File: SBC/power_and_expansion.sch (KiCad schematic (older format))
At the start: 19 parts, among them J1 VCC1, J10 GND3, J11 Expansion Bus, J2 GND1, J3 VCC2, J4 POWER, J5 GND2, J8 JTAG, J9 VCC3

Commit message: Preparation for Pluto v3.0
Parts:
- removed J8: JTAG, Connectors_IDC:IDC-Header_2x05_Pitch2.54mm_Straight, symbol conn:CONN_02X05
- removed MK2, MK5: Mounting_Hole, Mounting_Holes:MountingHole_3.2mm_M3_Pad, symbol mechanical:Mounting_Hole
- F1: footprint Fuse_Holders_and_Fuses:Fuseholder5x20_horiz_open_Schurter_0031_8201 -> Fuse:Fuseholder_Cylinder-5x20mm_Schurter_0031_8201_Horizontal_Open; symbol device:Fuse_Small -> pluto-rescue:Fuse_Small-device
- J1, J10, J2, J3, J5, J9: footprint Pin_Headers:Pin_Header_Straight_1x01_Pitch2.54mm -> Connector_PinHeader_2.54mm:PinHeader_1x01_P2.54mm_Vertical; symbol conn:TEST_1P -> pluto-rescue:TEST_1P-conn
- J11: footprint Connectors_IDC:IDC-Header_2x20_Pitch2.54mm_Straight -> Connector_IDC:IDC-Header_2x20_P2.54mm_Vertical
- J4: footprint Connectors_Molex:Molex_NanoFit_1x04x2.50mm_Angled -> Connector_Molex:Molex_Nano-Fit_105313-xx04_1x04_P2.50mm_Horizontal; symbol conn:CONN_01X04 -> pluto-rescue:CONN_01X04-conn
- MK1, MK3, MK4, MK6: footprint Mounting_Holes:MountingHole_3.2mm_M3_Pad -> MountingHole:MountingHole_3.2mm_M3_Pad; symbol mechanical:Mounting_Hole -> pluto-rescue:Mounting_Hole-mechanical
- R1: footprint Resistors_ThroughHole:R_Axial_DIN0411_L9.9mm_D3.6mm_P12.70mm_Horizontal -> Resistor_THT:R_Axial_DIN0411_L9.9mm_D3.6mm_P7.62mm_Vertical; symbol device:R_Small -> pluto-rescue:R_Small-device
- S1: symbol standard:SPDT -> pluto-rescue:SPDT-standard
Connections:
- net labels added: ~IO
- net labels removed: TCK, TDI, TDO, TMS, ~7FAX, ~7FCX
- wire segments 67 -> 56
- no-connect marks 6 -> 5
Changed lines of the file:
@@
 EESchema Schematic File Version 4
 LIBS:pluto-cache
-EELAYER 29 0
+EELAYER 30 0
 EELAYER END
 $Descr A4 11693 8268
@@
 $EndDescr
 $Comp
-L mechanical:Mounting_Hole MK2
-U 1 1 59149E60
-P 1825 3025
-F 0 "MK2" H 1825 3225 50  0000 C CNN
-F 1 "Mounting_Hole" H 1825 3150 50  0000 C CNN
-F 2 "Mounting_Holes:MountingHole_3.2mm_M3_Pad" H 1825 3025 50  0001 C CNN
-F 3 "" H 1825 3025 50  0001 C CNN
-	1    1825 3025
-	1    0    0    -1
-$EndComp
-$Comp
-L mechanical:Mounting_Hole MK3
+L pluto-rescue:Mounting_Hole-mechanical MK3
 U 1 1 59149E83
 P 1825 3450
 F 0 "MK3" H 1825 3650 50  0000 C CNN
 F 1 "Mounting_Hole" H 1825 3575 50  0000 C CNN
-F 2 "Mounting_Holes:MountingHole_3.2mm_M3_Pad" H 1825 3450 50  0001 C CNN
+F 2 "MountingHole:MountingHole_3.2mm_M3_Pad" H 1825 3450 50  0001 C CNN
 F 3 "" H 1825 3450 50  0001 C CNN
 	1    1825 3450
@@
 $EndComp
 $Comp
-L mechanical:Mounting_Hole MK1
+L pluto-rescue:Mounting_Hole-mechanical MK1
 U 1 1 5932DD04
-P 1125 3950
-F 0 "MK1" H 1125 4150 50  0000 C CNN
-F 1 "Mounting_Hole" H 1125 4075 50  0000 C CNN
-F 2 "Mounting_Holes:MountingHole_3.2mm_M3_Pad" H 1125 3950 50  0001 C CNN
-F 3 "" H 1125 3950 50  0001 C CNN
-	1    1125 3950
-	1    0    0    -1
-$EndComp
-$Comp
-L mechanical:Mounting_Hole MK4
+P 2625 3925
+F 0 "MK1" H 2625 4125 50  0000 C CNN
+F 1 "Mounting_Hole" H 2625 4050 50  0000 C CNN
+F 2 "MountingHole:MountingHole_3.2mm_M3_Pad" H 2625 3925 50  0001 C CNN
+F 3 "" H 2625 3925 50  0001 C CNN
+	1    2625 3925
+	1    0    0    -1
+$EndComp
+$Comp
+L pluto-rescue:Mounting_Hole-mechanical MK4
 U 1 1 5932DD62
 P 1825 3950
 F 0 "MK4" H 1825 4150 50  0000 C CNN
 F 1 "Mounting_Hole" H 1825 4075 50  0000 C CNN
-F 2 "Mounting_Holes:MountingHole_3.2mm_M3_Pad" H 1825 3950 50  0001 C CNN
+F 2 "MountingHole:MountingHole_3.2mm_M3_Pad" H 1825 3950 50  0001 C CNN
 F 3 "" H 1825 3950 50  0001 C CNN
 	1    1825 3950
@@
 $EndComp
 $Comp
-L conn:CONN_02X05 J8
-U 1 1 59F22BEE
-P 4275 3000
-F 0 "J8" H 4275 3300 50  0000 C CNN
-F 1 "JTAG" H 4275 2700 50  0000 C CNN
-F 2 "Connectors_IDC:IDC-Header_2x05_Pitch2.54mm_Straight" H 4275 1800 50  0001 C CNN
-F 3 "" H 4275 1800 50  0001 C CNN
-	1    4275 3000
-	1    0    0    -1
-$EndComp
-Text HLabel 3775 3000 0    60   Output ~ 0
-TDI
-Text HLabel 3775 3100 0    60   Input ~ 0
-TDO
-Text HLabel 3775 2800 0    60   Output ~ 0
-TCK
-Text HLabel 3775 2900 0    60   Output ~ 0
-TMS
-Wire Wire Line
-	3775 2800 4025 2800
-Wire Wire Line
-	3775 2900 4025 2900
-Wire Wire Line
-	3775 3000 4025 3000
-Wire Wire Line
-	3775 3100 4025 3100
-Wire Wire Line
-	4525 2800 4775 2800
-Wire Wire Line
-	4775 2900 4525 2900
-Wire Wire Line
-	4525 3000 4900 3000
-Wire Wire Line
-	4775 3100 4525 3100
-Wire Wire Line
-	4775 2675 4775 2800
-Connection ~ 4775 2800
-$Comp
-L power:GND #PWR024
-U 1 1 59F407A0
-P 4775 2675
-F 0 "#PWR024" H 4775 2425 50  0001 C CNN
-F 1 "GND" H 4775 2525 50  0000 C CNN
-F 2 "" H 4775 2675 50  0001 C CNN
-F 3 "" H 4775 2675 50  0001 C CNN
-	1    4775 2675
-	-1   0    0    1
-$EndComp
-$Comp
-L power:VCC #PWR025
-U 1 1 59F407C6
-P 4900 3000
-F 0 "#PWR025" H 4900 2850 50  0001 C CNN
-F 1 "VCC" V 4900 3175 50  0000 C CNN
-F 2 "" H 4900 3000 50  0001 C CNN
-F 3 "" H 4900 3000 50  0001 C CNN
-	1    4900 3000
-	0    1    1    0
-$EndComp
-Connection ~ 4775 2900
-NoConn ~ 4525 3200
-NoConn ~ 4025 3200
-$Comp
-L mechanical:Mounting_Hole MK5
-U 1 1 59F424EE
-P 2600 3000
-F 0 "MK5" H 2600 3200 50  0000 C CNN
-F 1 "Mounting_Hole" H 2600 3125 50  0000 C CNN
-F 2 "Mounting_Holes:MountingHole_3.2mm_M3_Pad" H 2600 3000 50  0001 C CNN
-F 3 "" H 2600 3000 50  0001 C CNN
-	1    2600 3000
-	1    0    0    -1
-$EndComp
-$Comp
-L mechanical:Mounting_Hole MK6
+L pluto-rescue:Mounting_Hole-mechanical MK6
 U 1 1 59F42548
 P 2600 3350
 F 0 "MK6" H 2600 3550 50  0000 C CNN
 F 1 "Mounting_Hole" H 2600 3475 50  0000 C CNN
-F 2 "Mounting_Holes:MountingHole_3.2mm_M3_Pad" H 2600 3350 50  0001 C CNN
+F 2 "MountingHole:MountingHole_3.2mm_M3_Pad" H 2600 3350 50  0001 C CNN
 F 3 "" H 2600 3350 50  0001 C CNN
 	1    2600 3350
@@
 $EndComp
 $Comp
-L conn:CONN_01X04 J4
+L pluto-rescue:CONN_01X04-conn J4
 U 1 1 5A1609CD
 P 7650 1725
 F 0 "J4" H 7650 1975 50  0000 C CNN
 F 1 "POWER" V 7750 1725 50  0000 C CNN
-F 2 "Connectors_Molex:Molex_NanoFit_1x04x2.50mm_Angled" H 7650 1725 50  0001 C CNN
+F 2 "Connector_Molex:Molex_Nano-Fit_105313-xx04_1x04_P2.50mm_Horizontal" H 7650 1725 50  0001 C CNN
 F 3 "" H 7650 1725 50  0001 C CNN
 	1    7650 1725
@@
 Connection ~ 7375 1675
 $Comp
-L device:Fuse_Small F1
+L pluto-rescue:Fuse_Small-device F1
 U 1 1 5A30BB96
 P 6800 1575
 F 0 "F1" H 6800 1515 50  0000 C CNN
 F 1 "1Amp" H 6800 1635 50  0000 C CNN
-F 2 "Fuse_Holders_and_Fuses:Fuseholder5x20_horiz_open_Schurter_0031_8201" H 6800 1575 50  0001 C CNN
+F 2 "Fuse:Fuseholder_Cylinder-5x20mm_Schurter_0031_8201_Horizontal_Open" H 6800 1575 50  0001 C CNN
 F 3 "" H 6800 1575 50  0001 C CNN
 	1    6800 1575
@@
 $EndComp
 $Comp
-L standard:SPDT S1
+L pluto-rescue:SPDT-standard S1
 U 1 1 5A30BD5A
 P 6425 1625
@@
 $EndComp
 $Comp
-L device:R_Small R1
+L pluto-rescue:R_Small-device R1
 U 1 1 5A30C649
 P 5625 1625
 F 0 "R1" V 5700 1575 50  0000 L CNN
 F 1 "1kOhm" V 5525 1525 50  0000 L CNN
-F 2 "Resistors_ThroughHole:R_Axial_DIN0411_L9.9mm_D3.6mm_P12.70mm_Horizontal" H 5625 1625 50  0001 C CNN
+F 2 "Resistor_THT:R_Axial_DIN0411_L9.9mm_D3.6mm_P7.62mm_Vertical" H 5625 1625 50  0001 C CNN
 F 3 "" H 5625 1625 50  0001 C CNN
 	1    5625 1625
@@
 	5425 1625 5525 1625
 $Comp
-L conn:TEST_1P J1
+L pluto-rescue:TEST_1P-conn J1
 U 1 1 5A30C731
 P 1450 5025
 F 0 "J1" H 1450 5295 50  0000 C CNN
 F 1 "VCC1" H 1450 5225 50  0000 C CNN
-F 2 "Pin_Headers:Pin_Header_Straight_1x01_Pitch2.54mm" H 1650 5025 50  0001 C CNN
+F 2 "Connector_PinHeader_2.54mm:PinHeader_1x01_P2.54mm_Vertical" H 1650 5025 50  0001 C CNN
 F 3 "" H 1650 5025 50  0001 C CNN
 	1    1450 5025
@@
 $EndComp
 $Comp
-L conn:TEST_1P J3
+L pluto-rescue:TEST_1P-conn J3
 U 1 1 5A30C776
 P 1775 5025
 F 0 "J3" H 1775 5295 50  0000 C CNN
 F 1 "VCC2" H 1775 5225 50  0000 C CNN
-F 2 "Pin_Headers:Pin_Header_Straight_1x01_Pitch2.54mm" H 1975 5025 50  0001 C CNN
+F 2 "Connector_PinHeader_2.54mm:PinHeader_1x01_P2.54mm_Vertical" H 1975 5025 50  0001 C CNN
 F 3 "" H 1975 5025 50  0001 C CNN
 	1    1775 5025
@@
 $EndComp
 $Comp
-L conn:TEST_1P J9
+L pluto-rescue:TEST_1P-conn J9
 U 1 1 5A30C7BB
 P 2125 5025
 F 0 "J9" H 2125 5295 50  0000 C CNN
 F 1 "VCC3" H 2125 5225 50  0000 C CNN
-F 2 "Pin_Headers:Pin_Header_Straight_1x01_Pitch2.54mm" H 2325 5025 50  0001 C CNN
+F 2 "Connector_PinHeader_2.54mm:PinHeader_1x01_P2.54mm_Vertical" H 2325 5025 50  0001 C CNN
 F 3 "" H 2325 5025 50  0001 C CNN
 	1    2125 5025
@@
 $EndComp
 $Comp
-L conn:TEST_1P J2
+L pluto-rescue:TEST_1P-conn J2
 U 1 1 5A30C814
 P 1450 5625
 F 0 "J2" H 1450 5895 50  0000 C CNN
 F 1 "GND1" H 1450 5825 50  0000 C CNN
-F 2 "Pin_Headers:Pin_Header_Straight_1x01_Pitch2.54mm" H 1650 5625 50  0001 C CNN
+F 2 "Connector_PinHeader_2.54mm:PinHeader_1x01_P2.54mm_Vertical" H 1650 5625 50  0001 C CNN
 F 3 "" H 1650 5625 50  0001 C CNN
 	1    1450 5625
@@
 $EndComp
 $Comp
-L conn:TEST_1P J5
+L pluto-rescue:TEST_1P-conn J5
 U 1 1 5A30C853
 P 1775 5625
 F 0 "J5" H 1775 5895 50  0000 C CNN
 F 1 "GND2" H 1775 5825 50  0000 C CNN
-F 2 "Pin_Headers:Pin_Header_Straight_1x01_Pitch2.54mm" H 1975 5625 50  0001 C CNN
+F 2 "Connector_PinHeader_2.54mm:PinHeader_1x01_P2.54mm_Vertical" H 1975 5625 50  0001 C CNN
 F 3 "" H 1975 5625 50  0001 C CNN
 	1    1775 5625
@@
 $EndComp
 $Comp
-L conn:TEST_1P J10
+L pluto-rescue:TEST_1P-conn J10
 U 1 1 5A30C89C
 P 2125 5625
 F 0 "J10" H 2125 5895 50  0000 C CNN
 F 1 "GND3" H 2125 5825 50  0000 C CNN
-F 2 "Pin_Headers:Pin_Header_Straight_1x01_Pitch2.54mm" H 2325 5625 50  0001 C CNN
+F 2 "Connector_PinHeader_2.54mm:PinHeader_1x01_P2.54mm_Vertical" H 2325 5625 50  0001 C CNN
 F 3 "" H 2325 5625 50  0001 C CNN
 	1    2125 5625
@@
 Text Label 6950 1575 0    60   ~ 0
 PWR_IN
-Text HLabel 9400 4775 2    60   Output ~ 0
-~7FCX
-Text HLabel 9400 4875 2    60   Output ~ 0
-~7FAX
 Text HLabel 8100 4875 0    60   Input ~ 0
 ~IRQ
@@
 F 0 "J11" H 8750 5075 50  0000 C CNN
 F 1 "Expansion Bus" V 8750 3925 50  0000 C CNN
-F 2 "Connectors_IDC:IDC-Header_2x20_Pitch2.54mm_Straight" H 8700 4075 50  0001 C CNN
+F 2 "Connector_IDC:IDC-Header_2x20_P2.54mm_Vertical" H 8700 4075 50  0001 C CNN
 F 3 "" H 8700 4075 50  0001 C CNN
 	1    8700 4075
@@
 Wire Wire Line
 	9000 4775 9400 4775
-Wire Wire Line
-	9000 4875 9400 4875
 Wire Wire Line
 	9000 4975 9400 4975
@@
 D7
 Wire Wire Line
-	4775 2800 4775 2900
-Wire Wire Line
-	4775 2900 4775 3100
-Wire Wire Line
 	7275 1675 7375 1675
 Wire Wire Line
@@
 Wire Wire Line
 	8750 5475 9000 5475
+NoConn ~ 9000 4875
+Text HLabel 9400 4775 2    60   Output ~ 0
+~IO
+$Comp
+L power:PWR_FLAG #FLG0101
+U 1 1 5D7FB0B7
+P 6200 1800
+F 0 "#FLG0101" H 6200 1875 50  0001 C CNN
+F 1 "PWR_FLAG" H 6200 1973 50  0000 C CNN
+F 2 "" H 6200 1800 50  0001 C CNN
+F 3 "~" H 6200 1800 50  0001 C CNN
+	1    6200 1800
+	-1   0    0    1
+$EndComp
+Wire Wire Line
+	6200 1800 6200 1625
 Wire Bus Line
 	9500 3175 9500 3875

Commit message: A better layout of PCB.
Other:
- note added: "IO ($7F60)"
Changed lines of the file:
@@
 Wire Bus Line
 	8000 3175 8000 4675
+Text Notes 9625 4825 0    60   ~ 12
+IO ($7F60)
 $EndSCHEMATC

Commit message: Converting to SMD of almost all components.
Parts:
- R1: footprint Resistor_THT:R_Axial_DIN0411_L9.9mm_D3.6mm_P7.62mm_Vertical -> Resistor_SMD:R_1206_3216Metric_Pad1.42x1.75mm_HandSolder
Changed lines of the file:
@@
 F 0 "R1" V 5700 1575 50  0000 L CNN
 F 1 "1kOhm" V 5525 1525 50  0000 L CNN
-F 2 "Resistor_THT:R_Axial_DIN0411_L9.9mm_D3.6mm_P7.62mm_Vertical" H 5625 1625 50  0001 C CNN
+F 2 "Resistor_SMD:R_1206_3216Metric_Pad1.42x1.75mm_HandSolder" H 5625 1625 50  0001 C CNN
 F 3 "" H 5625 1625 50  0001 C CNN
 	1    5625 1625
@@
 Wire Wire Line
 	6200 1800 6200 1625
+Text Notes 9625 4825 0    60   ~ 12
+IO ($7F60)
 Wire Bus Line
 	9500 3175 9500 3875
 Wire Bus Line
 	8000 3175 8000 4675
-Text Notes 9625 4825 0    60   ~ 12
-IO ($7F60)
 $EndSCHEMATC

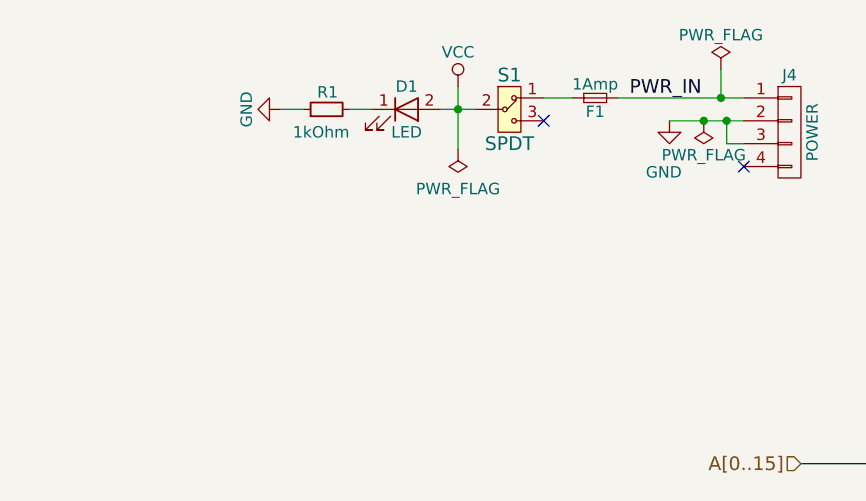
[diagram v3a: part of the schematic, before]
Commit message: Layout of PCB continues.
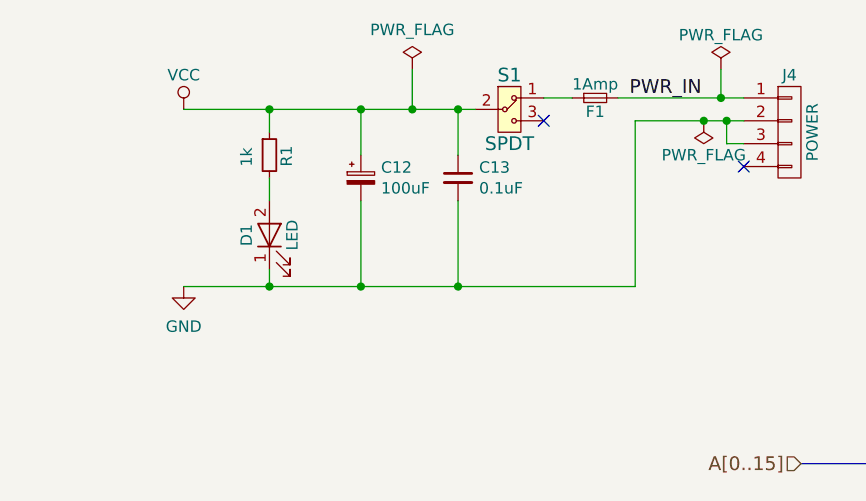
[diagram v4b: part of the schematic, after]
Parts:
- added C12: 100uF, Capacitor_Tantalum_SMD:CP_EIA-3528-15_AVX-H_Pad1.50x2.35mm_HandSolder, symbol Device:CP_Small
- added C13: 0.1uF, Capacitor_SMD:C_0805_2012Metric_Pad1.15x1.40mm_HandSolder, symbol Device:C_Small
- F1: footprint Fuse:Fuseholder_Cylinder-5x20mm_Schurter_0031_8201_Horizontal_Open -> Grotto:FUSE_0154004.DR
- R1: value 1kOhm -> 1k
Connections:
- net GND: now also D1.1 (K), C12.2, C13.2; no longer R1.1
- net VCC: now also R1.1, C12.1, C13.1; no longer D1.2 (A)
- net at R1.2: now also D1.2 (A); no longer D1.1 (K)
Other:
- moved on the sheet: D1, R1
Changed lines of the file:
@@
 $EndComp
-Wire Wire Line
-	7125 1675 7275 1675
 Wire Wire Line
 	7375 1775 7450 1775
@@
 L power:VCC #PWR026
 U 1 1 5A160A6E
-P 6200 1525
-F 0 "#PWR026" H 6200 1375 50  0001 C CNN
-F 1 "VCC" H 6200 1675 50  0000 C CNN
-F 2 "" H 6200 1525 50  0001 C CNN
-F 3 "" H 6200 1525 50  0001 C CNN
-	1    6200 1525
+P 5000 1625
+F 0 "#PWR026" H 5000 1475 50  0001 C CNN
+F 1 "VCC" H 5000 1775 50  0000 C CNN
+F 2 "" H 5000 1625 50  0001 C CNN
+F 3 "" H 5000 1625 50  0001 C CNN
+	1    5000 1625
 	1    0    0    -1
 $EndComp
@@
 L power:GND #PWR027
 U 1 1 5A160AE2
-P 7125 1675
-F 0 "#PWR027" H 7125 1425 50  0001 C CNN
-F 1 "GND" H 7100 1450 50  0000 C CNN
-F 2 "" H 7125 1675 50  0001 C CNN
-F 3 "" H 7125 1675 50  0001 C CNN
-	1    7125 1675
+P 5000 2400
+F 0 "#PWR027" H 5000 2150 50  0001 C CNN
+F 1 "GND" H 5000 2225 50  0000 C CNN
+F 2 "" H 5000 2400 50  0001 C CNN
+F 3 "" H 5000 2400 50  0001 C CNN
+	1    5000 2400
 	1    0    0    -1
 $EndComp
@@
 Wire Wire Line
 	7375 1675 7375 1775
-Connection ~ 7275 1675
 NoConn ~ 7450 1875
 Connection ~ 7375 1675
@@
 F 0 "F1" H 6800 1515 50  0000 C CNN
 F 1 "1Amp" H 6800 1635 50  0000 C CNN
-F 2 "Fuse:Fuseholder_Cylinder-5x20mm_Schurter_0031_8201_Horizontal_Open" H 6800 1575 50  0001 C CNN
+F 2 "Grotto:FUSE_0154004.DR" H 6800 1575 50  0001 C CNN
 F 3 "" H 6800 1575 50  0001 C CNN
 	1    6800 1575
@@
 L pluto-rescue:LED D1
 U 1 1 5A30C5EA
-P 5975 1625
-F 0 "D1" H 5975 1725 50  0000 C CNN
-F 1 "LED" H 5975 1525 50  0000 C CNN
-F 2 "LEDs:LED_D3.0mm" H 5975 1625 50  0001 C CNN
-F 3 "" H 5975 1625 50  0001 C CNN
-	1    5975 1625
-	1    0    0    -1
+P 5375 2175
+F 0 "D1" H 5375 2275 50  0000 C CNN
+F 1 "LED" H 5375 2075 50  0000 C CNN
+F 2 "LEDs:LED_D3.0mm" H 5375 2175 50  0001 C CNN
+F 3 "" H 5375 2175 50  0001 C CNN
+	1    5375 2175
+	0    -1   -1   0
 $EndComp
 $Comp
 L pluto-rescue:R_Small-device R1
 U 1 1 5A30C649
-P 5625 1625
-F 0 "R1" V 5700 1575 50  0000 L CNN
-F 1 "1kOhm" V 5525 1525 50  0000 L CNN
-F 2 "Resistor_SMD:R_1206_3216Metric_Pad1.42x1.75mm_HandSolder" H 5625 1625 50  0001 C CNN
-F 3 "" H 5625 1625 50  0001 C CNN
-	1    5625 1625
-	0    -1   -1   0
-$EndComp
-$Comp
-L power:GND #PWR032
-U 1 1 5A30C680
-P 5425 1625
-F 0 "#PWR032" H 5425 1375 50  0001 C CNN
-F 1 "GND" H 5425 1475 50  0000 C CNN
-F 2 "" H 5425 1625 50  0001 C CNN
-F 3 "" H 5425 1625 50  0001 C CNN
-	1    5425 1625
-	0    1    1    0
-$EndComp
-Wire Wire Line
-	6125 1625 6200 1625
-Wire Wire Line
-	5725 1625 5825 1625
-Wire Wire Line
-	5425 1625 5525 1625
+P 5375 1825
+F 0 "R1" V 5450 1775 50  0000 L CNN
+F 1 "1k" V 5275 1775 50  0000 L CNN
+F 2 "Resistor_SMD:R_1206_3216Metric_Pad1.42x1.75mm_HandSolder" H 5375 1825 50  0001 C CNN
+F 3 "" H 5375 1825 50  0001 C CNN
+	1    5375 1825
+	1    0    0    -1
+$EndComp
 $Comp
 L pluto-rescue:TEST_1P-conn J1
@@
 Wire Wire Line
 	6700 1575 6575 1575
-Wire Wire Line
-	6200 1525 6200 1625
-Connection ~ 6200 1625
 Text Label 6950 1575 0    60   ~ 0
 PWR_IN
@@
 	7350 1575 7450 1575
 Wire Wire Line
-	6200 1625 6275 1625
-Wire Wire Line
 	8750 2775 9000 2775
 Wire Wire Line
@@
 L power:PWR_FLAG #FLG0101
 U 1 1 5D7FB0B7
-P 6200 1800
-F 0 "#FLG0101" H 6200 1875 50  0001 C CNN
-F 1 "PWR_FLAG" H 6200 1973 50  0000 C CNN
-F 2 "" H 6200 1800 50  0001 C CNN
-F 3 "~" H 6200 1800 50  0001 C CNN
-	1    6200 1800
-	-1   0    0    1
-$EndComp
-Wire Wire Line
-	6200 1800 6200 1625
+P 6000 1450
+F 0 "#FLG0101" H 6000 1525 50  0001 C CNN
+F 1 "PWR_FLAG" H 6000 1623 50  0000 C CNN
+F 2 "" H 6000 1450 50  0001 C CNN
+F 3 "~" H 6000 1450 50  0001 C CNN
+	1    6000 1450
+	1    0    0    -1
+$EndComp
 Text Notes 9625 4825 0    60   ~ 12
 IO ($7F60)
+Wire Wire Line
+	7275 1675 6975 1675
+Connection ~ 7275 1675
+Wire Wire Line
+	6000 1450 6000 1625
+Connection ~ 6000 1625
+Wire Wire Line
+	6000 1625 5775 1625
+Wire Wire Line
+	6000 1625 6200 1625
+$Comp
+L Device:CP_Small C12
+U 1 1 5D92EB72
+P 5775 1925
+F 0 "C12" H 5863 1971 50  0000 L CNN
+F 1 "100uF" H 5863 1880 50  0000 L CNN
+F 2 "Capacitor_Tantalum_SMD:CP_EIA-3528-15_AVX-H_Pad1.50x2.35mm_HandSolder" H 5775 1925 50  0001 C CNN
+F 3 "~" H 5775 1925 50  0001 C CNN
+	1    5775 1925
+	1    0    0    -1
+$EndComp
+$Comp
+L Device:C_Small C13
+U 1 1 5D92F51B
+P 6200 1925
+F 0 "C13" H 6292 1971 50  0000 L CNN
+F 1 "0.1uF" H 6292 1880 50  0000 L CNN
+F 2 "Capacitor_SMD:C_0805_2012Metric_Pad1.15x1.40mm_HandSolder" H 6200 1925 50  0001 C CNN
+F 3 "~" H 6200 1925 50  0001 C CNN
+	1    6200 1925
+	1    0    0    -1
+$EndComp
+Wire Wire Line
+	6200 1825 6200 1625
+Connection ~ 6200 1625
+Wire Wire Line
+	6200 1625 6275 1625
+Wire Wire Line
+	5775 1825 5775 1625
+Connection ~ 5775 1625
+Wire Wire Line
+	5775 1625 5375 1625
+Wire Wire Line
+	5775 2025 5775 2400
+Wire Wire Line
+	6200 2025 6200 2400
+Wire Wire Line
+	6975 2400 6200 2400
+Wire Wire Line
+	6975 1675 6975 2400
+Connection ~ 6200 2400
+Wire Wire Line
+	6200 2400 5775 2400
+Connection ~ 5775 2400
+Wire Wire Line
+	5775 2400 5375 2400
+Wire Wire Line
+	5375 1725 5375 1625
+Connection ~ 5375 1625
+Wire Wire Line
+	5375 1625 5000 1625
+Wire Wire Line
+	5375 1925 5375 2025
+Wire Wire Line
+	5375 2325 5375 2400
 Wire Bus Line
 	9500 3175 9500 3875
 Wire Bus Line
 	8000 3175 8000 4675
+Connection ~ 5375 2400
+Wire Wire Line
+	5375 2400 5000 2400
 $EndSCHEMATC
